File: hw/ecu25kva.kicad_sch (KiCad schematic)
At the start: 0 parts

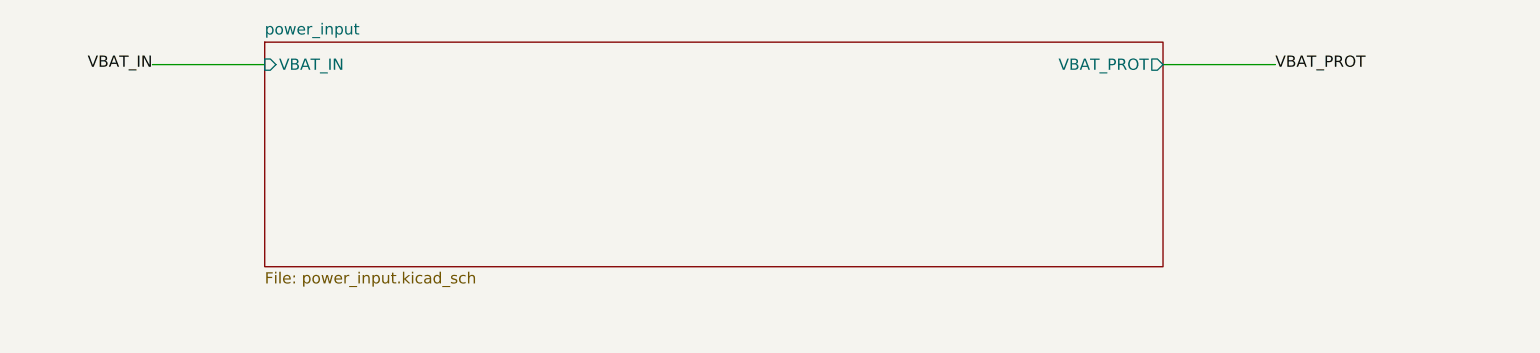
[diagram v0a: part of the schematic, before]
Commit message: Choose the negative clamp's control, and fix the latch a passing check hid
TLV3201-Q1 comparator into a UCC27517A-Q1 driver, both from retrieved
datasheets. The comparator's 52 mA would take about half a microsecond
to charge the clamp FET's gate; the driver's 4 A takes nanoseconds.

THE CLAMP LATCHED, AND run_sim.py SAID IT WAS RESOLVED. The model engaged
the active clamp near VIN = +0.08 V and released it only above +0.12 V.
At the end of every negative pulse the source returns to +13.5 V and
drives current back through the still-on clamp: 1.35 A through 5 mOhm is
6.7 mV, never reaching the release threshold. So the clamp stayed on and
shorted the source for the rest of the run -- clamped VIN sat at
0.0067 V while the Schottky-only branch recovered to 11.25 V. The check
measured only the clamp branch's MINIMUM. A recovery check, added first
and seen to fail on both pulse 1 and pulse 3a, is now permanent. With a
real battery in place of the test generator's 10 ohm, that is a dead
short after the first negative pulse.

The clamp is a low-side ideal diode -- anode ground, cathode VIN -- and
now engages below -100 mV and releases above -6.8 mV. Both thresholds sit
below ground, and a single-supply comparator has no negative reference,
so the sense node is lifted: 10k from VIN and 499k from 5V_MAIN put it at
0.9804 x VIN + 98.2 mV. Reference: 10k to ground, 536k from the output.
The drawn network and the model's thresholds are now tied by arithmetic
checks. 523k, the first value, put the worst-case release at +0.5 mV --
above zero, and the claim that said otherwise was reworded by moving the
resistor rather than the words.

THE WINDOW BEFORE IT ENGAGES IS A NUMBER NOW, AND IT IS INSIDE THE
RATING. With ~100 ns of delay (50 + 23 ns max, plus gate charge) VIN
crosses -100 mV, keeps falling ~90 ns, and bottoms at -0.177 V -- 1.70x
inside the LM5164's -0.3 V. The previous -0.068 V was optimistic by 2.6x:
at the default timestep ngspice committed the hysteretic switch on a
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
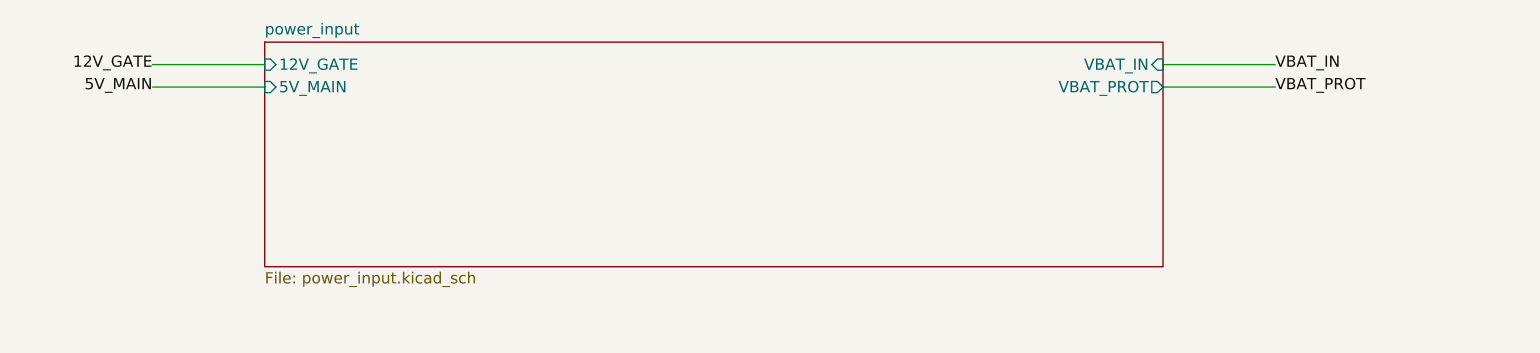
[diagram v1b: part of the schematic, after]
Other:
- sheet power_input ports: added 12V_GATE, 5V_MAIN; removed none
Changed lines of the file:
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@@
       (effects (font (size 1.27 1.27)) (justify left) hide)
     )
-    (pin "VBAT_IN" input (at 45.00 30.54 180)
-      (effects (font (size 1.27 1.27)) (justify left))
-    )
-    (pin "VBAT_PROT" output (at 146.60 30.54 0)
+    (pin "12V_GATE" input (at 45.00 30.54 180)
+      (effects (font (size 1.27 1.27)) (justify left))
+    )
+    (pin "5V_MAIN" input (at 45.00 33.08 180)
+      (effects (font (size 1.27 1.27)) (justify left))
+    )
+    (pin "VBAT_IN" input (at 146.60 30.54 0)
+      (effects (font (size 1.27 1.27)) (justify right))
+    )
+    (pin "VBAT_PROT" output (at 146.60 33.08 0)
       (effects (font (size 1.27 1.27)) (justify right))
     )
@@
     (stroke (width 0) (type default))
   )
-  (label "VBAT_IN" (at 32.30 30.54 180)
+  (label "12V_GATE" (at 32.30 30.54 180)
+    (effects (font (size 1.27 1.27)) (justify right))
+  )
+  (wire (pts (xy 45.00 33.08) (xy 32.30 33.08))
+    (stroke (width 0) (type default))
+  )
+  (label "5V_MAIN" (at 32.30 33.08 180)
     (effects (font (size 1.27 1.27)) (justify right))
   )
@@
     (stroke (width 0) (type default))
   )
-  (label "VBAT_PROT" (at 159.30 30.54 0)
+  (label "VBAT_IN" (at 159.30 30.54 0)
     (effects (font (size 1.27 1.27)) (justify left))
   )
+  (wire (pts (xy 146.60 33.08) (xy 159.30 33.08))
+    (stroke (width 0) (type default))
+  )
+  (label "VBAT_PROT" (at 159.30 33.08 0)
+    (effects (font (size 1.27 1.27)) (justify left))
+  )

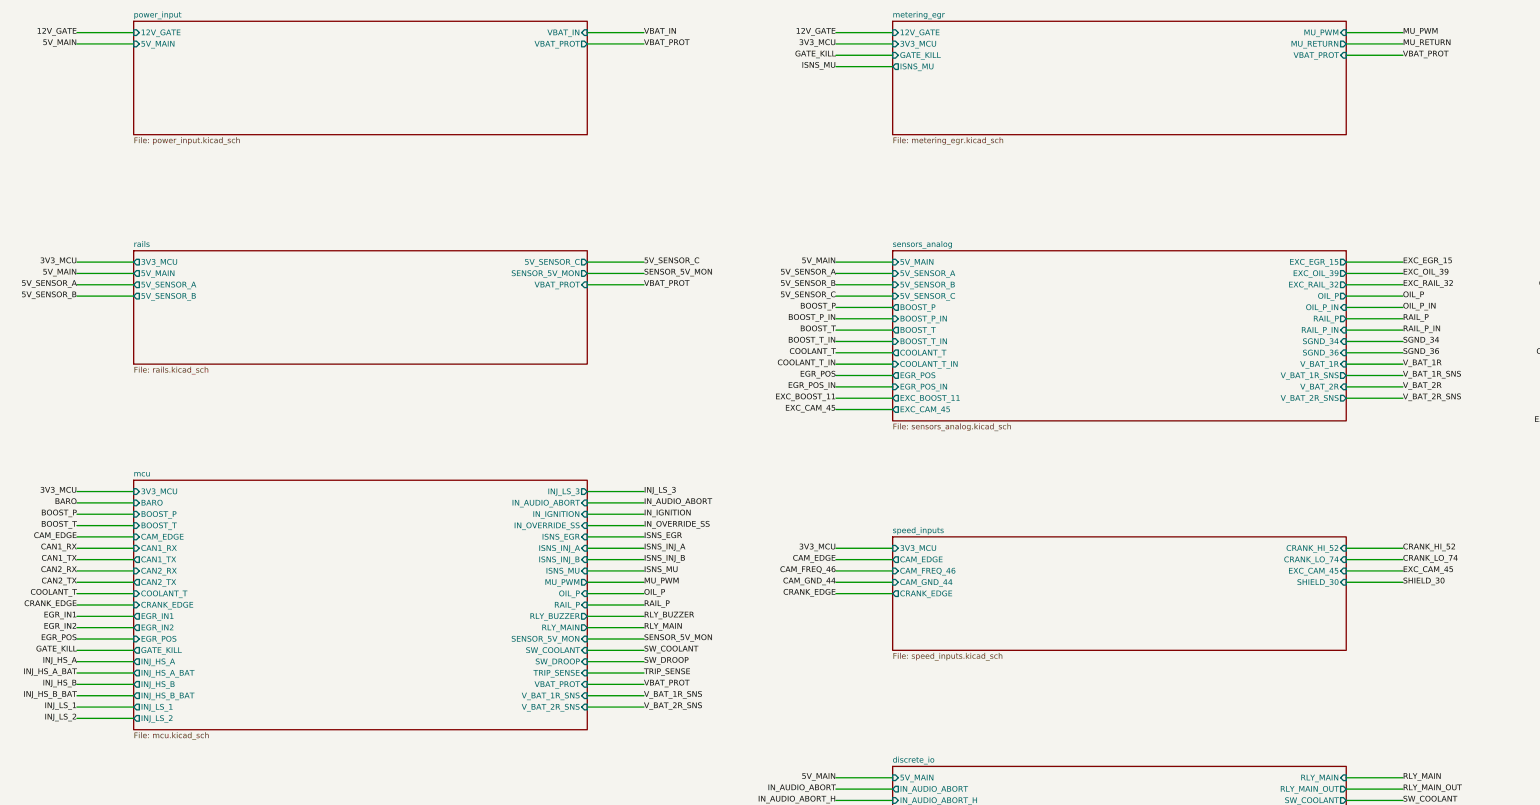
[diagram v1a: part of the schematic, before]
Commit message: Draw the EGR bridge: discrete, two AUIRS2184S, coast asserted by copper
Blocked since 20 September on one datasheet: DRV8873-Q1 had exactly the
decoded interface EGR-DRIVER asks for, and a 40 V VM absolute maximum
against a rail that reaches 73.3 V. Integrated automotive bridges cap at
40-45 V as a class. So the bridge is discrete: four 100 V N-FETs, <=20
mOhm, headroom over the 6.4 A stall.

THE DECODE COMES FROM THE DRIVER'S STRUCTURE, NOT A LOGIC GATE.
egr_hbridge.cir found that two logic lines wired to two diagonal switch
pairs short the bridge at 270 A with both asserted, and said "a per-leg
dead time is not enough on its own -- the fault here is a logic state".
AUIRS2184S has ONE input per leg: IN high puts HO on, IN low puts LO on,
with cross-conduction prevention and ~400 ns deadtime. Each leg's high
and low are exclusive by construction, so the 270 A state -- both inputs
high -- becomes a high-side brake.

Same Infineon family as the injector drivers, chosen the opposite way
for the opposite reason: the 2181's lack of interlock is what lets it
fire an injector, whose switches are in series with a coil; the 2184's
interlock is what makes a bridge leg safe.

COAST IS ASSERTED BY COPPER. egr_hbridge.cir argues coast, not brake, is
the safe state: a return spring closes the valve if the motor is let go.
Both drivers' SD-bar share EGR_SD, pulled down 10k, so with the enable
pin Hi-Z at reset both legs are off. A kill FET on the same node gives
coast on GATE_KILL with no MCU involvement. That enable costs one MCU
pin: PTB10, FTM3_CH2, same timer as EGR_IN1/IN2, PE=0/PS=0 at reset.
Pin map 41 -> 42 committed, 87 -> 86 spare.

One 20 mOhm shunt in the shared low-side return into an INA181A1-Q1
(2.56 V at a 6.4 A stall -> PTD22). It reads the drive phase; low-side
recirculation circulates between the two low FETs and misses it, so
firmware samples at the centre of the on-time -- recorded on the part.

The project netlist names the bridge nodes EGR_HIGH_59 and EGR_LO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
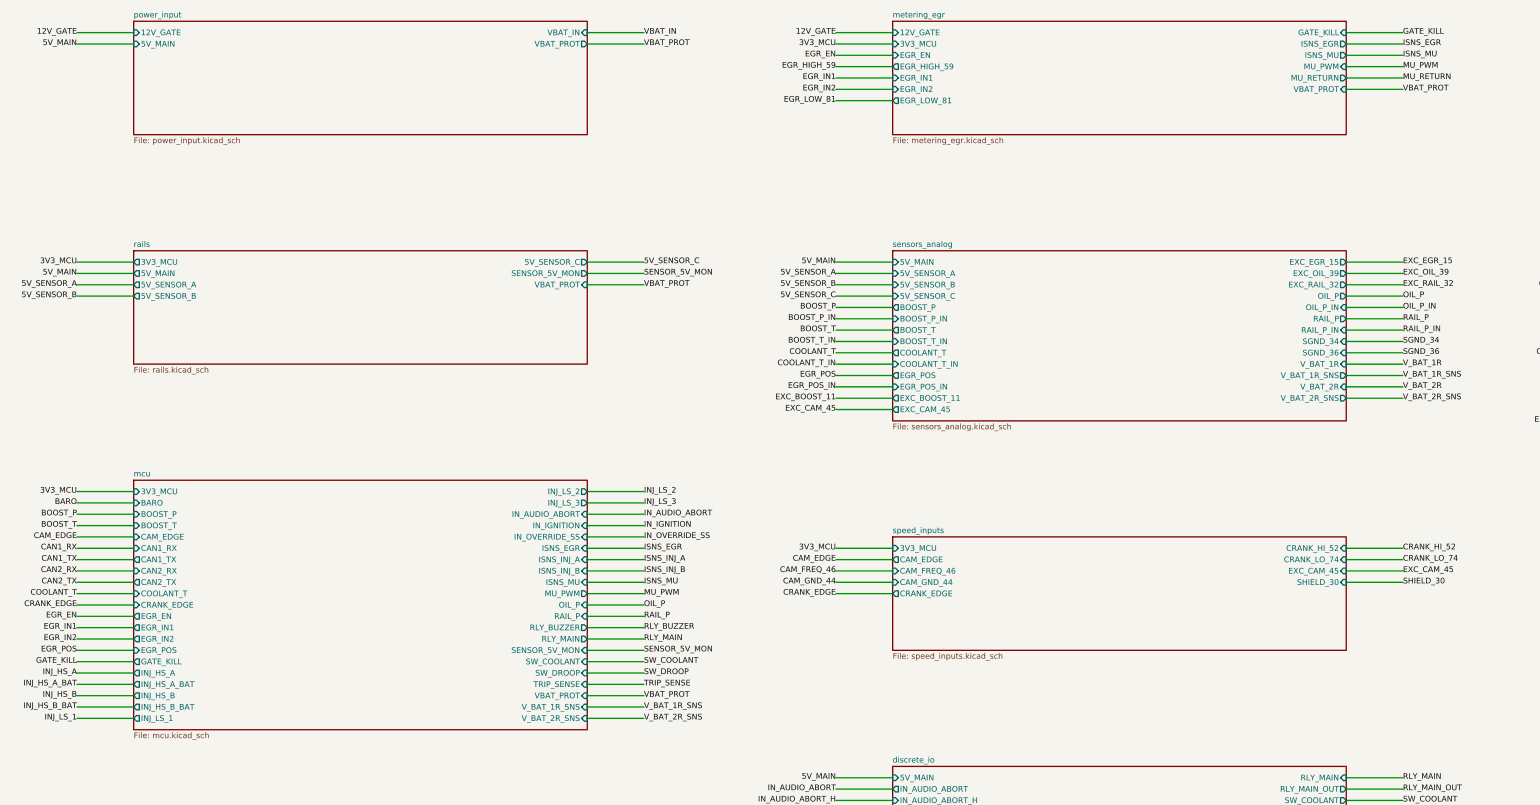
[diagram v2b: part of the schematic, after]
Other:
- sheet mcu ports: added EGR_EN; removed none
- sheet metering_egr ports: added EGR_EN, EGR_HIGH_59, EGR_IN1, EGR_IN2, EGR_LOW_81, ISNS_EGR; removed none

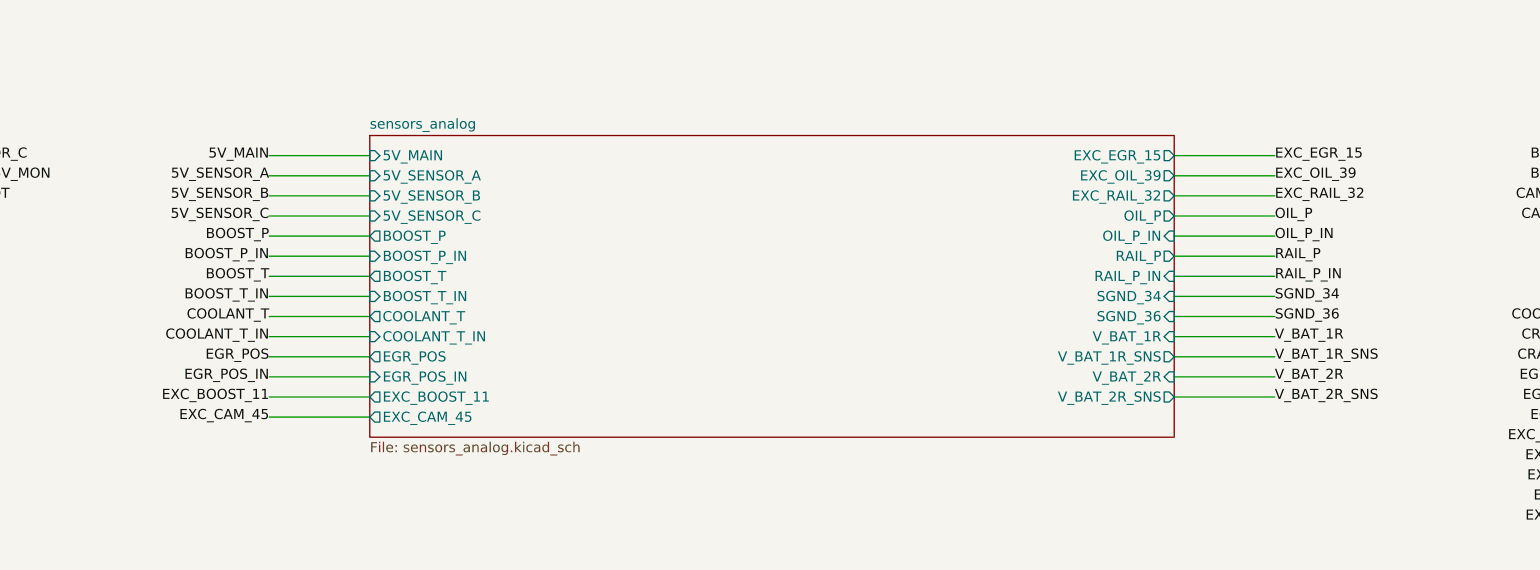
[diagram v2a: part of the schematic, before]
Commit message: Draw the onboard barometric sensor; one open end left, and it needs the machine
Spec sec.7 deviation 2 adds the baro on purpose: on-PCB behind a vented
port, costs nothing in harness terms, improves fuelling correction.

NXP MPXHZ6115A6T1, from the retrieved MPXA6115A series data sheet
(Rev. 7.3): 15-115 kPa, VOUT = VS(0.009P - 0.095), pins 1 DNC / 2 VS /
3 GND / 4 VOUT / 5-8 DNC, case 98ARH99066A -- a footprint KiCad ships,
whose pads 1-8 were checked against the datasheet's pin table.

Supplied from 5V_MAIN, which SENSOR_5V_MON already measures, so the
reading is ratiometric-correctable with no new channel. Through the same
10k/16k divider the sheet's other 5 V channels use: 2.51 V at sea level,
1.92 V at 2000 m, and no zener -- every other channel on that sheet
arrives from the harness and this one never leaves the board.

NOT STATED AEC-Q100 in the retrieved datasheet, and that is recorded
rather than assumed away. Infineon's KP236 is listed automotive-qualified
(40-115 kPa) and would be the choice, but its datasheet did not resolve
by any route -- Mouser timed out twice, Infineon's own host redirected --
and it is a footprint change, not a drop-in.

Open ends 2 -> 1. TRIP_LOOP remains, and no part closes it: it is a new
signal, not on the OEM diagram, and needs a connector pin AND a harness
wire -- field-brief task 5.2.

ONE DISAGREEMENT FOUND ON THE WAY, recorded in status.md for a decision
rather than fixed: spec sec.7 deviation 1 says the ECU uses functionally
split sealed connectors with an adapter harness to the OEM loom, and
hw/connector.kicad_sch draws the OEM 94-way on the board. The electrical
content is identical either way; the physical part and the adapter are a
scope decision.

24/24 blocks, 24/24 netlist checks, 44 supply pins decoupled.

Co-Authored-By: Claude Opus 5 <noreply@anthropic.com>
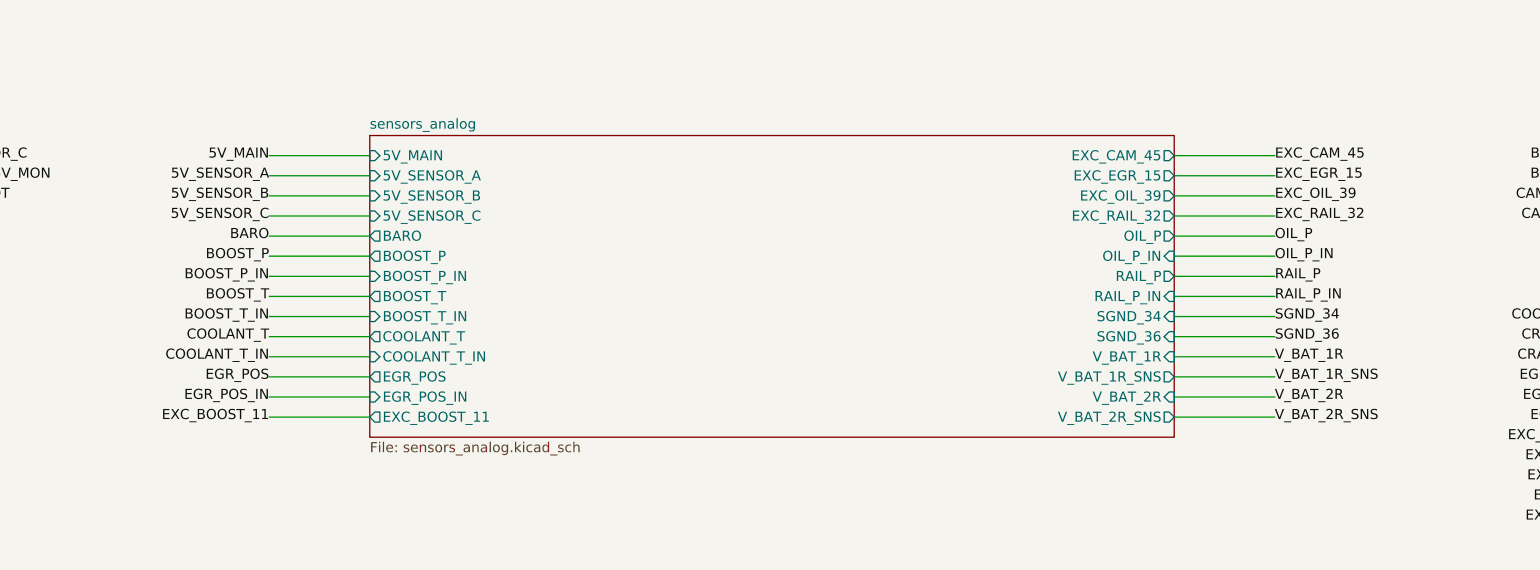
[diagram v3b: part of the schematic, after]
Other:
- sheet sensors_analog ports: added BARO; removed none
